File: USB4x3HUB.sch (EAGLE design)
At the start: 115 parts, among them IC1 TUSB2036, IC10 SN74LVC1G139DCTR, IC2 FSUSB74MPX, IC3 TPS2041C, IC4 TPS2041C, IC5 TPS2041C, IC6 3.3V, IC7 5V, IC8 5V, IC9 5V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

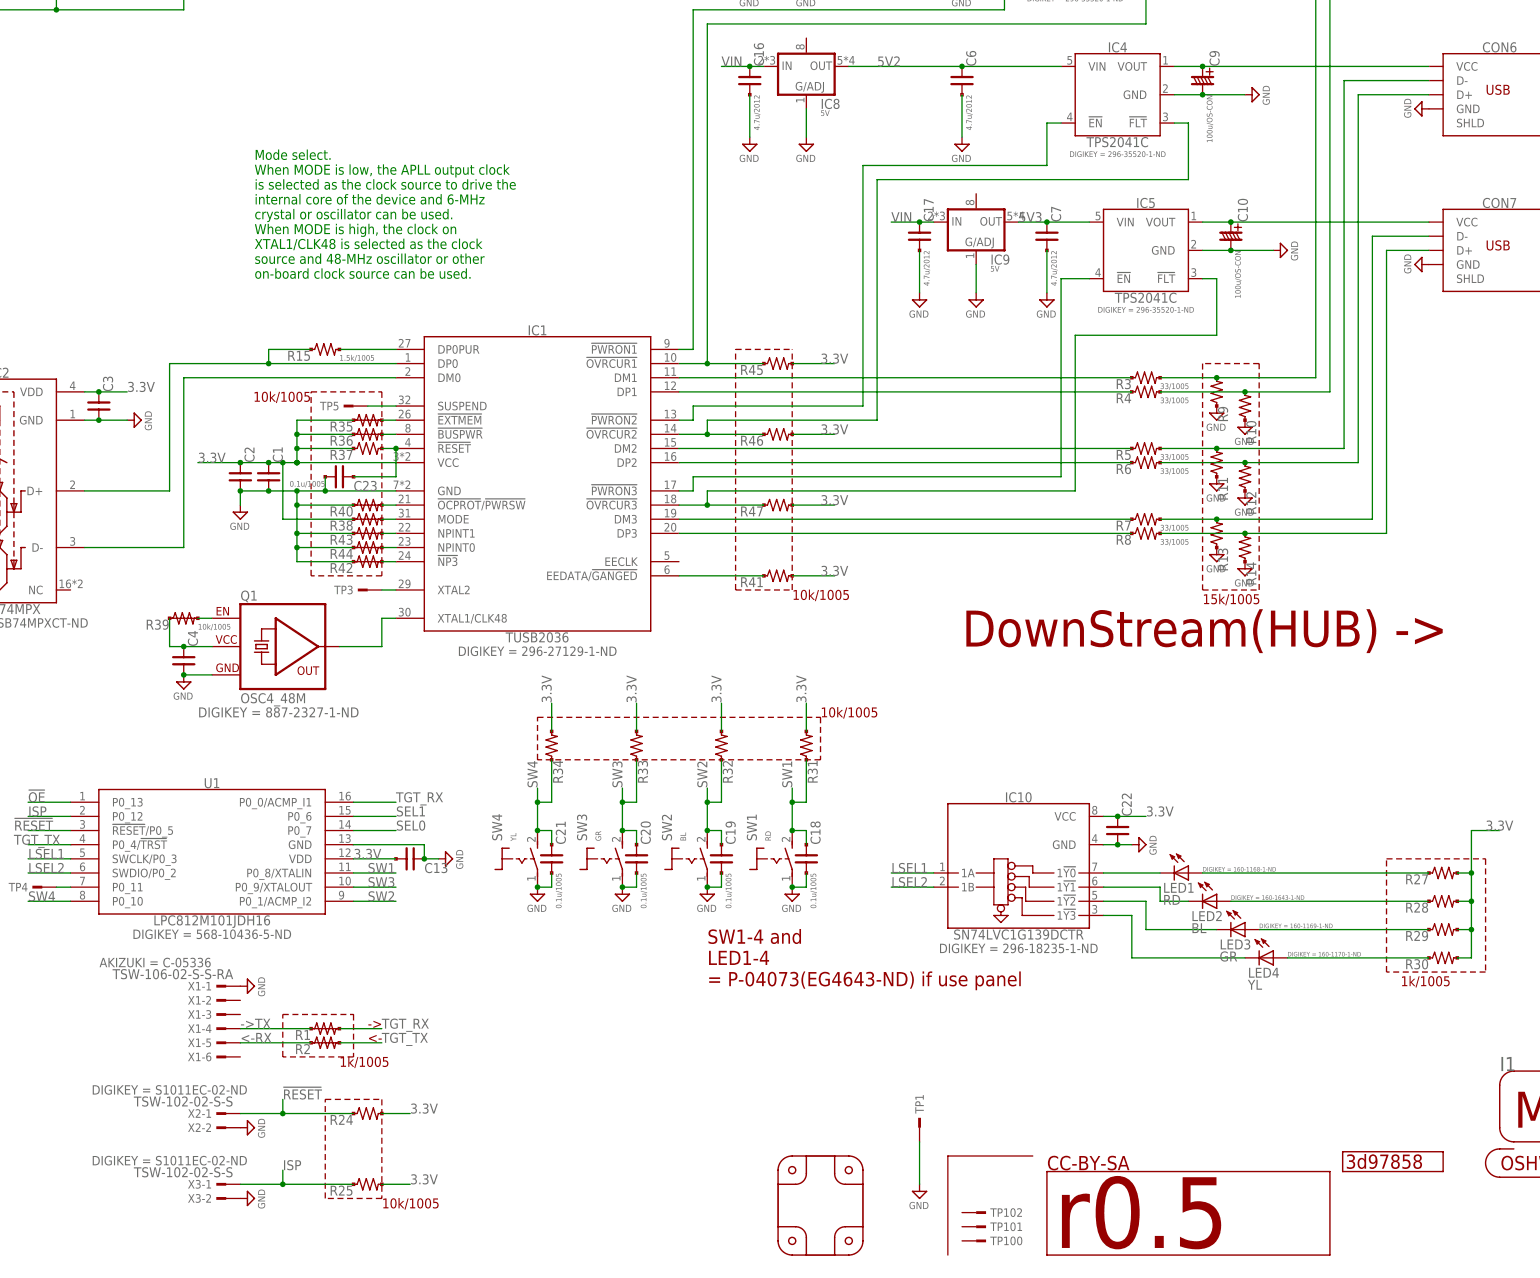
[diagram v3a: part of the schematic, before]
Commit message: apply library updates; regenerate BOM
- add SMD_PAD/TH_PAD attributes
- update some supplier attributes
  - update BOM based on this update
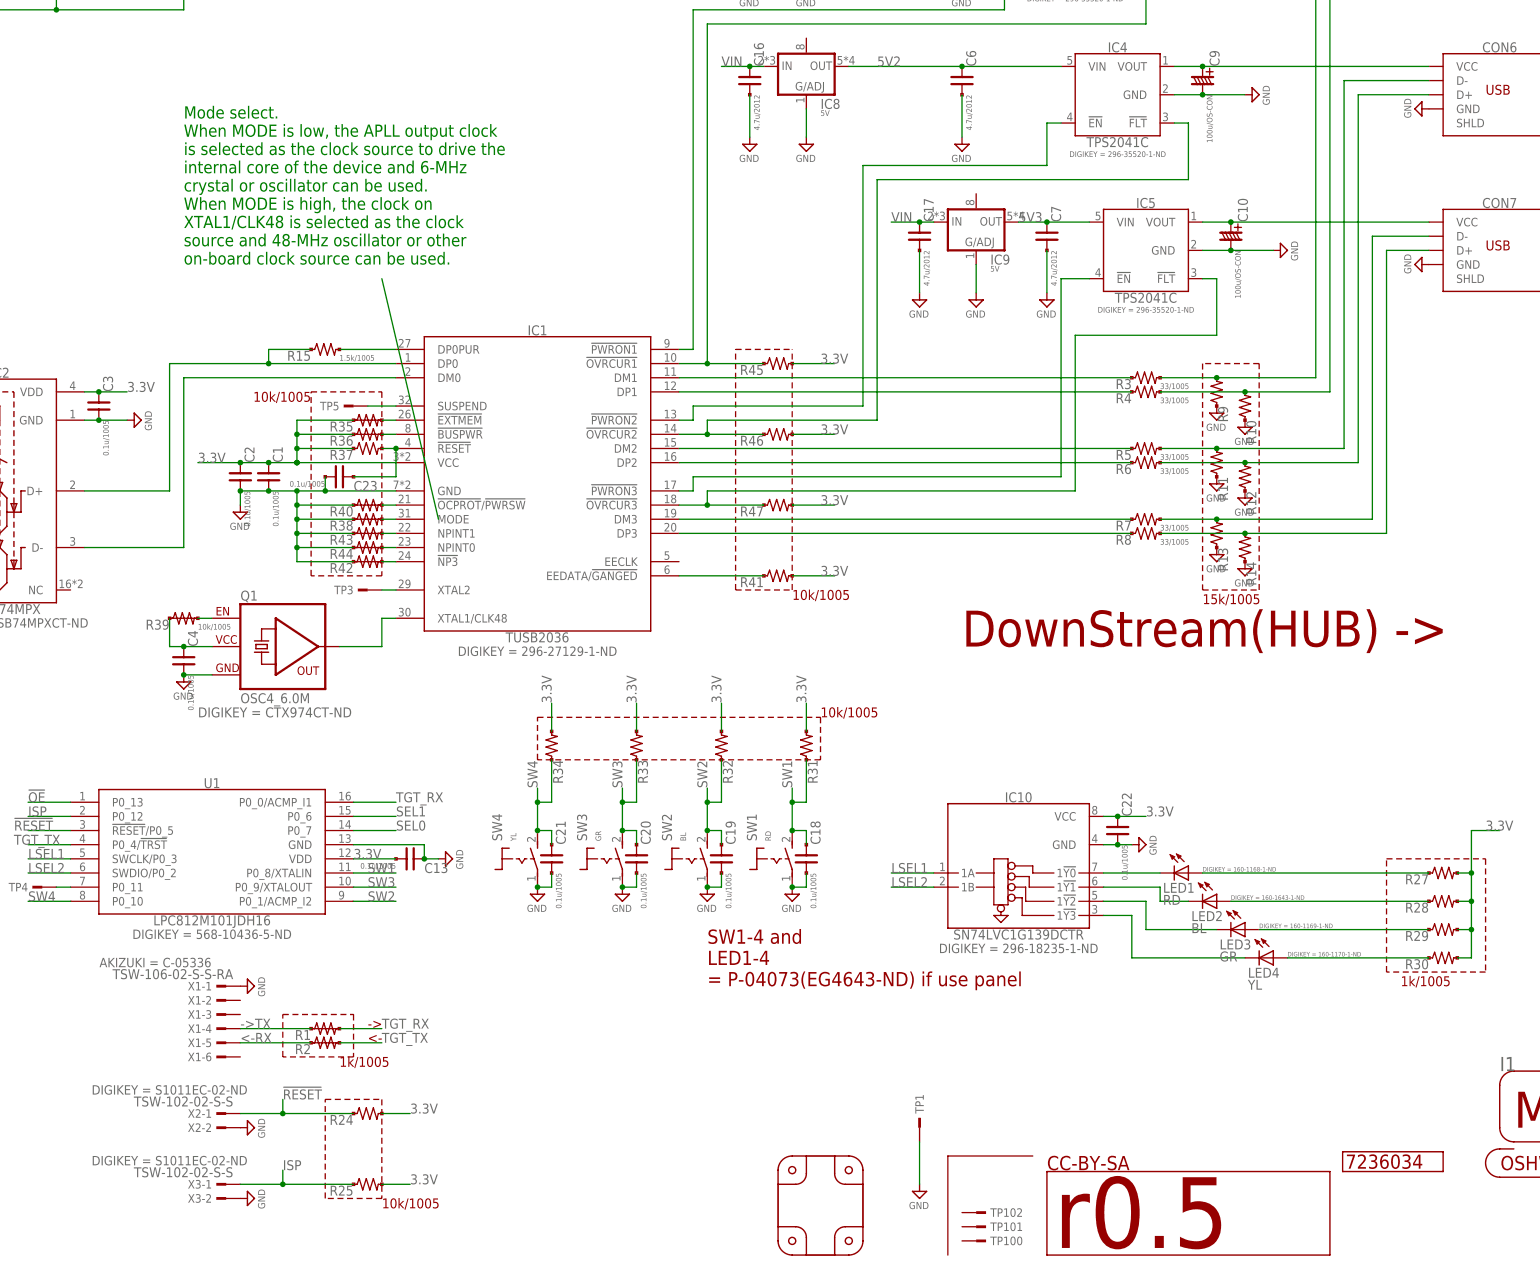
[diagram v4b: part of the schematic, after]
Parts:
- C1, C13, C2, C22, C3, C4: value (none) -> 0.1u/1005
- GIT1: value 3d97858 -> 7236034
- Q1: value OSC4_48M -> OSC4_6.0M; device mylib:OSC4_48M -> mylib:OSC4_6.0M
- R10, R11, R12, R13, R14, R9: value (none) -> 15k/1005
- R24, R25, R31, R32, R33, R34, R37, R41, R45, R46, R47: value (none) -> 10k/1005
- R27, R28, R29, R30: value (none) -> 1k/1005
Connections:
- net 3.3V: no longer R38.1
- net GND: now also R38.1

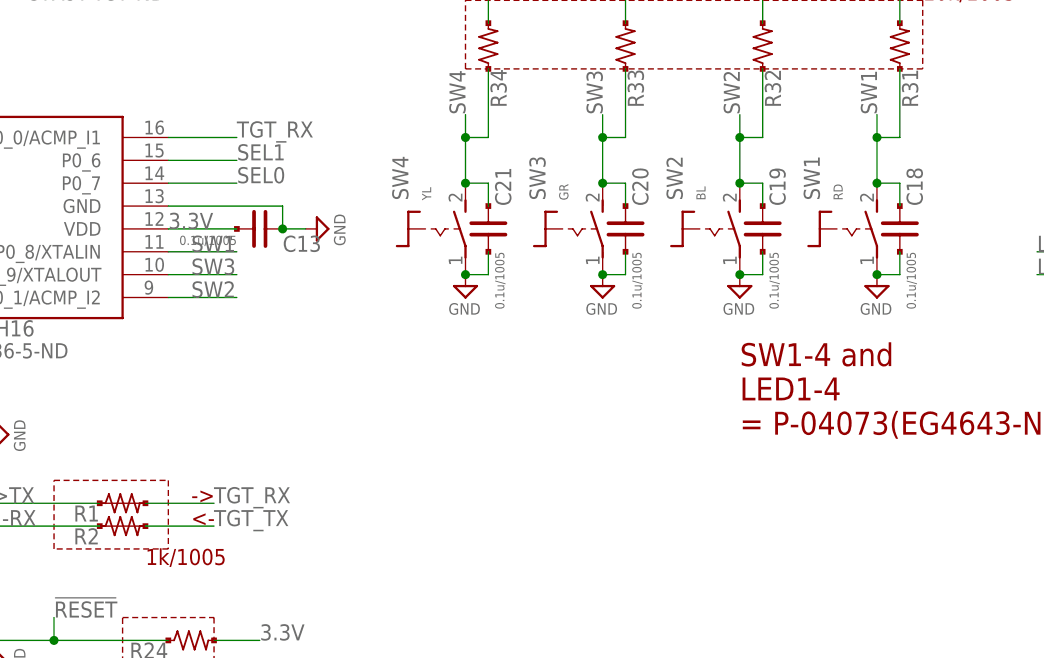
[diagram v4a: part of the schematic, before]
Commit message: [BRD] replace SW1-4;add pin headers for daughter board
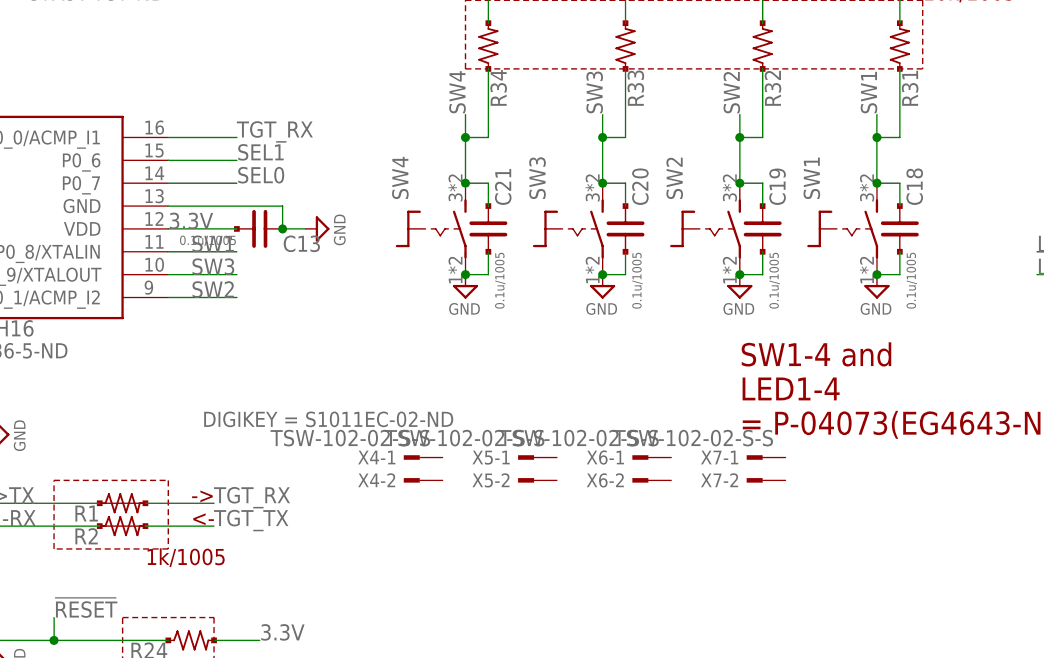
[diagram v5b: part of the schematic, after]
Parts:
- added X4, X5, X6, X7: TSW-102-02-S-S, con-samtec.local:TSW-102-02-S-S
- SW1: value RD -> (none); device mylib:TACTSW2_FSM2JMTR -> mylib:TACTSW2_WH_SKRPACE010
- SW2: value BL -> (none); device mylib:TACTSW2_FSM2JMTR -> mylib:TACTSW2_WH_SKRPACE010
- SW3: value GR -> (none); device mylib:TACTSW2_FSM2JMTR -> mylib:TACTSW2_WH_SKRPACE010
- SW4: value YL -> (none); device mylib:TACTSW2_FSM2JMTR -> mylib:TACTSW2_WH_SKRPACE010
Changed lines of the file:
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@@
 <part name="J1" library="mylib" deviceset="CON_DCJACK" device="_C1604"/>
 <part name="U1" library="mylib" deviceset="IC_LPC81X_16" device="_JDH16" value="LPC812M101JDH16"/>
-<part name="SW4" library="mylib" deviceset="TACTSW2_*" device="FSM2JMTR" value="YL"/>
-<part name="SW3" library="mylib" deviceset="TACTSW2_*" device="FSM2JMTR" value="GR"/>
-<part name="SW2" library="mylib" deviceset="TACTSW2_*" device="FSM2JMTR" value="BL"/>
-<part name="SW1" library="mylib" deviceset="TACTSW2_*" device="FSM2JMTR" value="RD"/>
 <part name="SUPPLY1" library="mylib" deviceset="GND" device=""/>
 <part name="SUPPLY2" library="mylib" deviceset="GND" device=""/>
@@
 <part name="P4" library="mylib" deviceset="PCB_CORNER" device=""/>
 <part name="TP5" library="mylib" deviceset="TESTPAD" device=""/>
+<part name="X4" library="con-samtec.local" deviceset="TSW-102-02-S-S" device="" value="TSW-102-02-S-S">
+<attribute name="NOT_COMPONENT" value="YES"/>
+</part>
+<part name="X5" library="con-samtec.local" deviceset="TSW-102-02-S-S" device="" value="TSW-102-02-S-S">
+<attribute name="NOT_COMPONENT" value="YES"/>
+</part>
+<part name="X6" library="con-samtec.local" deviceset="TSW-102-02-S-S" device="" value="TSW-102-02-S-S">
+<attribute name="NOT_COMPONENT" value="YES"/>
+</part>
+<part name="X7" library="con-samtec.local" deviceset="TSW-102-02-S-S" device="" value="TSW-102-02-S-S">
+<attribute name="NOT_COMPONENT" value="YES"/>
+</part>
+<part name="SW4" library="mylib" deviceset="TACTSW2_*" device="_SKRPACE010" technology="WH"/>
+<part name="SW3" library="mylib" deviceset="TACTSW2_*" device="_SKRPACE010" technology="WH"/>
+<part name="SW2" library="mylib" deviceset="TACTSW2_*" device="_SKRPACE010" technology="WH"/>
+<part name="SW1" library="mylib" deviceset="TACTSW2_*" device="_SKRPACE010" technology="WH"/>
 </parts>
 <sheets>
@@
 <attribute name="DIGIKEY" x="139.7" y="63.5" size="1.6764" layer="96" align="top-center" display="both"/>
 </instance>
-<instance part="SW4" gate="G$1" x="195.58" y="76.2"/>
-<instance part="SW3" gate="G$1" x="210.82" y="76.2"/>
-<instance part="SW2" gate="G$1" x="226.06" y="76.2"/>
-<instance part="SW1" gate="G$1" x="241.3" y="76.2"/>
 <instance part="SUPPLY1" gate="GND" x="88.9" y="226.06"/>
 <instance part="SUPPLY2" gate="GND" x="144.78" y="137.16"/>
@@
 <instance part="P4" gate="G$1" x="251.46" y="10.16"/>
 <instance part="TP5" gate="1" x="165.1" y="157.48" rot="R180"/>
+<instance part="X4" gate="-1" x="193.04" y="50.8" rot="MR0">
+<attribute name="DIGIKEY" x="182.88" y="55.88" size="1.6764" layer="96" rot="MR180" align="bottom-center" display="both"/>
+</instance>
+<instance part="X4" gate="-2" x="193.04" y="48.26" rot="MR0"/>
+<instance part="X5" gate="-1" x="205.74" y="50.8" rot="MR0"/>
+<instance part="X5" gate="-2" x="205.74" y="48.26" rot="MR0"/>
+<instance part="X6" gate="-1" x="218.44" y="50.8" rot="MR0"/>
+<instance part="X6" gate="-2" x="218.44" y="48.26" rot="MR0"/>
+<instance part="X7" gate="-1" x="231.14" y="50.8" rot="MR0"/>
+<instance part="X7" gate="-2" x="231.14" y="48.26" rot="MR0"/>
+<instance part="SW4" gate="G$1" x="195.58" y="76.2"/>
+<instance part="SW3" gate="G$1" x="210.82" y="76.2"/>
+<instance part="SW2" gate="G$1" x="226.06" y="76.2"/>
+<instance part="SW1" gate="G$1" x="241.3" y="76.2"/>
 </instances>
 <busses>
@@
 </segment>
 <segment>
-<pinref part="SW4" gate="G$1" pin="P"/>
 <pinref part="SUPPLY5" gate="GND" pin="GND"/>
 <pinref part="C21" gate="G$1" pin="2"/>
@@
 <wire x1="200.66" y1="71.12" x2="200.66" y2="73.66" width="0.1524" layer="91"/>
 <junction x="198.12" y="71.12"/>
-</segment>
-<segment>
-<pinref part="SW3" gate="G$1" pin="P"/>
+<pinref part="SW4" gate="G$1" pin="P"/>
+</segment>
+<segment>
 <pinref part="SUPPLY6" gate="GND" pin="GND"/>
 <pinref part="C20" gate="G$1" pin="2"/>
@@
 <wire x1="215.9" y1="71.12" x2="215.9" y2="73.66" width="0.1524" layer="91"/>
 <junction x="213.36" y="71.12"/>
-</segment>
-<segment>
-<pinref part="SW2" gate="G$1" pin="P"/>
+<pinref part="SW3" gate="G$1" pin="P"/>
+</segment>
+<segment>
 <pinref part="SUPPLY7" gate="GND" pin="GND"/>
 <pinref part="C19" gate="G$1" pin="2"/>
@@
 <wire x1="231.14" y1="71.12" x2="231.14" y2="73.66" width="0.1524" layer="91"/>
 <junction x="228.6" y="71.12"/>
-</segment>
-<segment>
-<pinref part="SW1" gate="G$1" pin="P"/>
+<pinref part="SW2" gate="G$1" pin="P"/>
+</segment>
+<segment>
 <pinref part="SUPPLY8" gate="GND" pin="GND"/>
 <pinref part="C18" gate="G$1" pin="2"/>
@@
 <wire x1="246.38" y1="71.12" x2="246.38" y2="73.66" width="0.1524" layer="91"/>
 <junction x="243.84" y="71.12"/>
+<pinref part="SW1" gate="G$1" pin="P"/>
 </segment>
 <segment>
@@
 <segment>
 <wire x1="243.84" y1="88.9" x2="243.84" y2="86.36" width="0.1524" layer="91"/>
-<pinref part="SW1" gate="G$1" pin="S"/>
 <label x="243.84" y="88.9" size="1.778" layer="95" rot="R90"/>
 <pinref part="R31" gate="G$1" pin="1"/>
@@
 <wire x1="246.38" y1="81.28" x2="246.38" y2="78.74" width="0.1524" layer="91"/>
 <junction x="243.84" y="81.28"/>
+<pinref part="SW1" gate="G$1" pin="S"/>
 </segment>
 <segment>
@@
 <segment>
 <wire x1="228.6" y1="88.9" x2="228.6" y2="86.36" width="0.1524" layer="91"/>
-<pinref part="SW2" gate="G$1" pin="S"/>
 <label x="228.6" y="88.9" size="1.778" layer="95" rot="R90"/>
 <wire x1="228.6" y1="86.36" x2="228.6" y2="81.28" width="0.1524" layer="91"/>
@@
 <wire x1="231.14" y1="81.28" x2="231.14" y2="78.74" width="0.1524" layer="91"/>
 <junction x="228.6" y="81.28"/>
+<pinref part="SW2" gate="G$1" pin="S"/>
 </segment>
 <segment>
@@
 <segment>
 <wire x1="213.36" y1="88.9" x2="213.36" y2="86.36" width="0.1524" layer="91"/>
-<pinref part="SW3" gate="G$1" pin="S"/>
 <label x="213.36" y="88.9" size="1.778" layer="95" rot="R90"/>
 <wire x1="213.36" y1="86.36" x2="213.36" y2="81.28" width="0.1524" layer="91"/>
@@
 <wire x1="215.9" y1="81.28" x2="215.9" y2="78.74" width="0.1524" layer="91"/>
 <junction x="213.36" y="81.28"/>
+<pinref part="SW3" gate="G$1" pin="S"/>
 </segment>
 <segment>
@@
 <segment>
 <wire x1="198.12" y1="88.9" x2="198.12" y2="86.36" width="0.1524" layer="91"/>
-<pinref part="SW4" gate="G$1" pin="S"/>
 <label x="198.12" y="88.9" size="1.778" layer="95" rot="R90"/>
 <wire x1="198.12" y1="86.36" x2="198.12" y2="81.28" width="0.1524" layer="91"/>
@@
 <wire x1="200.66" y1="81.28" x2="200.66" y2="78.74" width="0.1524" layer="91"/>
 <junction x="198.12" y="81.28"/>
-</segment>
-<segment>
+<pinref part="SW4" gate="G$1" pin="S"/>
+</segment>
+<segment>
